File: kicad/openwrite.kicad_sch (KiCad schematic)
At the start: 147 parts, among them J1 raspberry-pi-zero-with-test-p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, SW71 SW_SPST, U1 kb2040, U2 powerboost-1000c, U3 waveshare-2in-lcd-st7789v

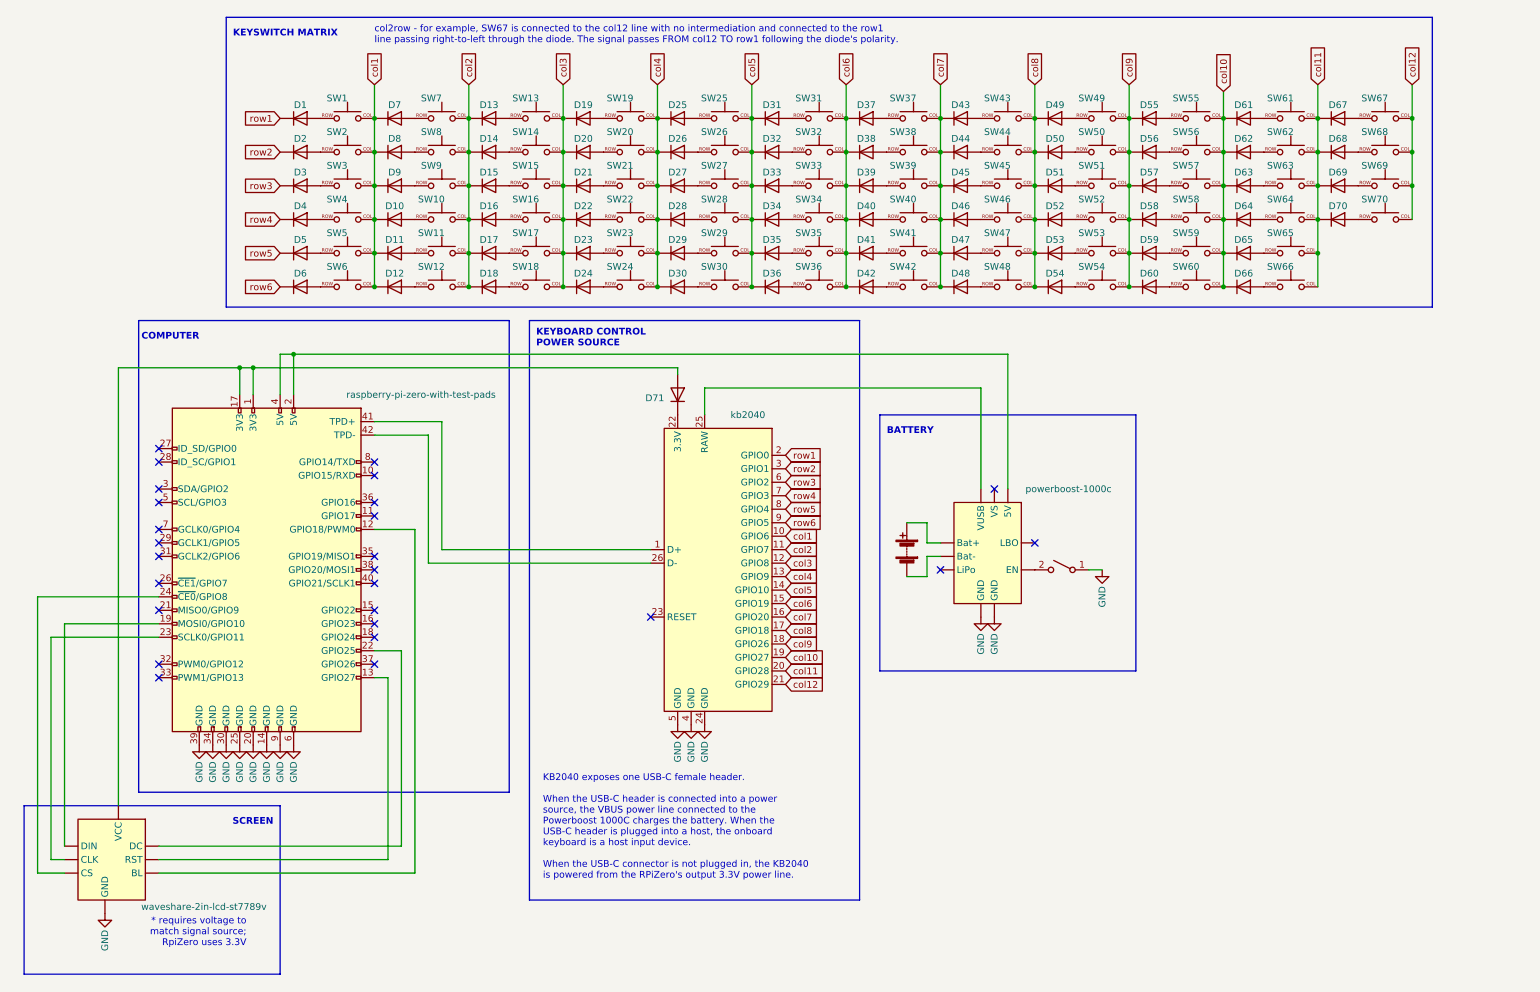
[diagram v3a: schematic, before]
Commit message: row connected to all row elements
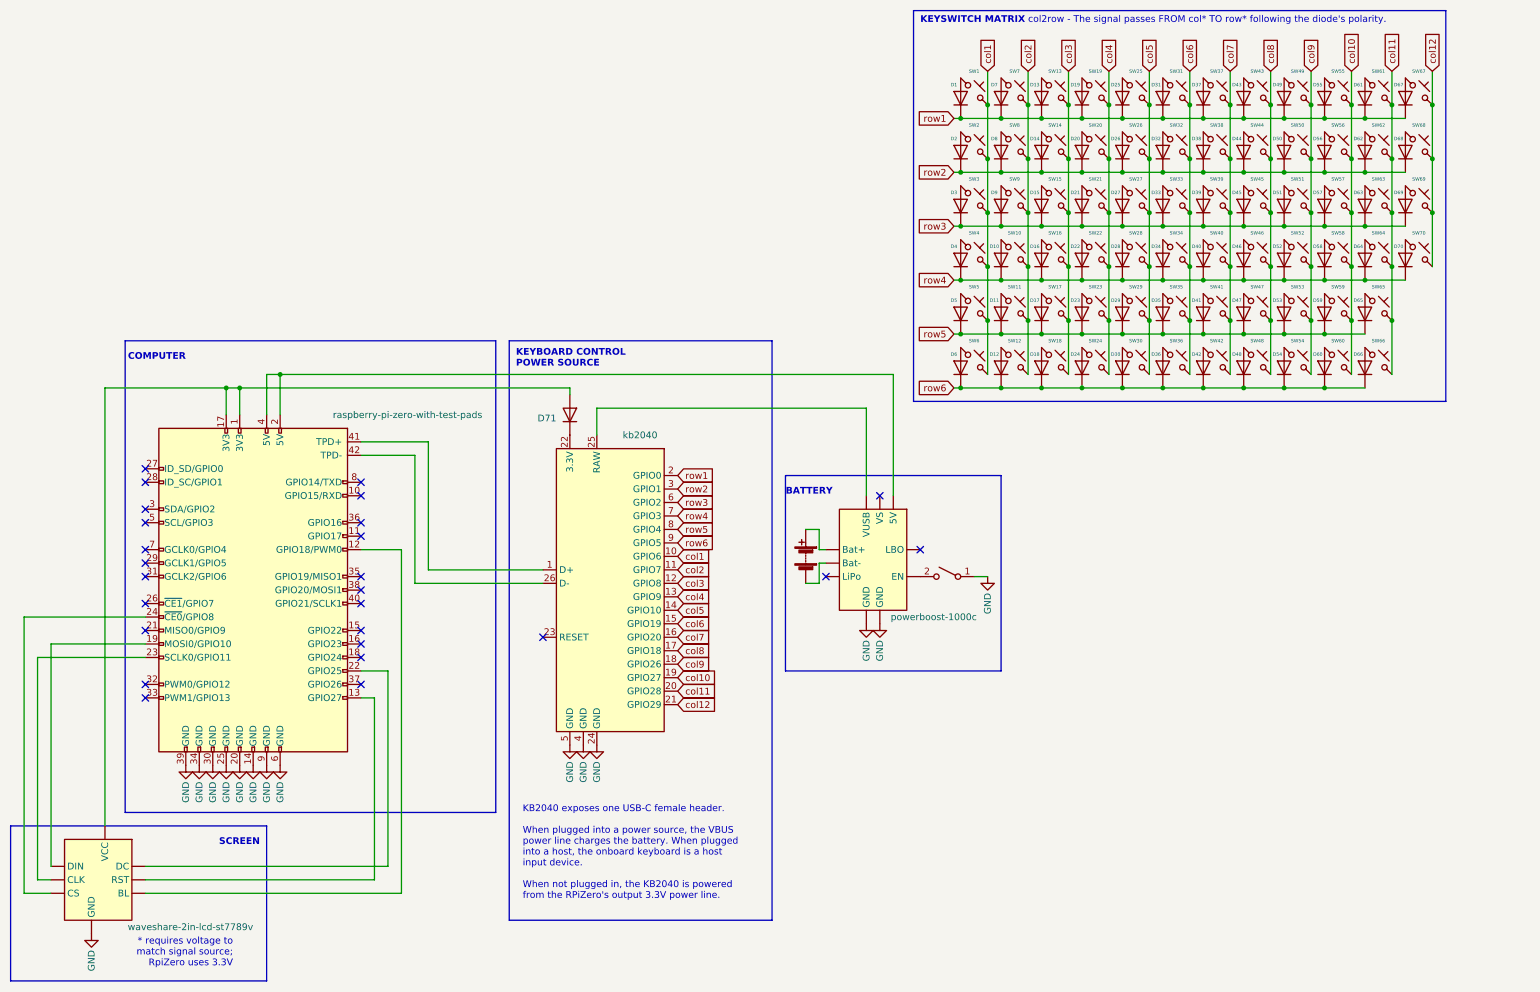
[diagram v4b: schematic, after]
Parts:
- D1, D10, D11, D12, D13, D14, D15, D16, D17, D18, D19, D2, D20, D21, D22, D23, D24, D25, D26, D27, D28, D29, D3, D30, D31, D32, D33, D34, D35, D36, D37, D38, D39, D4, D40, D41, D42, D43, D44, D45, D46, D47, D48, D49, D5, D50, D51, D52, D53, D54, D55, D56, D57, D58, D59, D6, D60, D61, D62, D63, D64, D65, D66, D67, D68, D69, D7, D70, D71, D8, D9: footprint Diode_THT:D_DO-35_SOD27_P7.62mm_Horizontal -> openwrite:diode-1N4148FS-ND
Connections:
- net col1: no longer D10.D1 (K), D11.D1 (K), D12.D1 (K), D7.D1 (K), D8.D1 (K), D9.D1 (K)
- net col10: no longer D61.D1 (K), D62.D1 (K), D63.D1 (K), D64.D1 (K), D65.D1 (K), D66.D1 (K)
- net col11: no longer D67.D1 (K), D68.D1 (K), D69.D1 (K), D70.D1 (K)
- net col2: no longer D13.D1 (K), D14.D1 (K), D15.D1 (K), D16.D1 (K), D17.D1 (K), D18.D1 (K)
- net col3: no longer D19.D1 (K), D20.D1 (K), D21.D1 (K), D22.D1 (K), D23.D1 (K), D24.D1 (K)
- net col4: no longer D25.D1 (K), D26.D1 (K), D27.D1 (K), D28.D1 (K), D29.D1 (K), D30.D1 (K)
- net col5: no longer D31.D1 (K), D32.D1 (K), D33.D1 (K), D34.D1 (K), D35.D1 (K), D36.D1 (K)
- net col6: no longer D37.D1 (K), D38.D1 (K), D39.D1 (K), D40.D1 (K), D41.D1 (K), D42.D1 (K)
- net col7: no longer D43.D1 (K), D44.D1 (K), D45.D1 (K), D46.D1 (K), D47.D1 (K), D48.D1 (K)
- net col8: no longer D49.D1 (K), D50.D1 (K), D51.D1 (K), D52.D1 (K), D53.D1 (K), D54.D1 (K)
- net col9: no longer D55.D1 (K), D56.D1 (K), D57.D1 (K), D58.D1 (K), D59.D1 (K), D60.D1 (K)
- net row1: now also D1.1, D13.1, D19.1, D25.1, D31.1, D37.1, D43.1, D49.1, D55.1, D61.1, D67.1, D7.1; no longer D1.D1 (K)
- net row2: now also D14.1, D2.1, D20.1, D26.1, D32.1, D38.1, D44.1, D50.1, D56.1, D62.1, D68.1, D8.1; no longer D2.D1 (K)
- net row3: now also D15.1, D21.1, D27.1, D3.1, D33.1, D39.1, D45.1, D51.1, D57.1, D63.1, D69.1, D9.1; no longer D3.D1 (K)
- net row4: now also D10.1, D16.1, D22.1, D28.1, D34.1, D4.1, D40.1, D46.1, D52.1, D58.1, D64.1, D70.1; no longer D4.D1 (K)
- net row5: now also D11.1, D17.1, D23.1, D29.1, D35.1, D41.1, D47.1, D5.1, D53.1, D59.1, D65.1; no longer D5.D1 (K)
- net row6: now also D12.1, D18.1, D24.1, D30.1, D36.1, D42.1, D48.1, D54.1, D6.1, D60.1, D66.1; no longer D6.D1 (K)
- net at SW29.ROW: now also D29.2; no longer D29.D2 (A)
- net at SW49.ROW: now also D49.2; no longer D49.D2 (A)
- net at SW70.ROW: now also D70.2; no longer D70.D2 (A)
- net at SW50.ROW: now also D50.2; no longer D50.D2 (A)
- net at SW15.ROW: now also D15.2; no longer D15.D2 (A)
- net at SW64.ROW: now also D64.2; no longer D64.D2 (A)
- net at SW47.ROW: now also D47.2; no longer D47.D2 (A)
- net at SW62.ROW: now also D62.2; no longer D62.D2 (A)
- net at SW40.ROW: now also D40.2; no longer D40.D2 (A)
- net at SW68.ROW: now also D68.2; no longer D68.D2 (A)
- net at SW2.ROW: now also D2.2; no longer D2.D2 (A)
- net at SW58.ROW: now also D58.2; no longer D58.D2 (A)
- net at SW26.ROW: now also D26.2; no longer D26.D2 (A)
- net at SW30.ROW: now also D30.2; no longer D30.D2 (A)
- net at SW51.ROW: now also D51.2; no longer D51.D2 (A)
- net at SW5.ROW: now also D5.2; no longer D5.D2 (A)
- net at SW16.ROW: now also D16.2; no longer D16.D2 (A)
- net at SW56.ROW: now also D56.2; no longer D56.D2 (A)
- net at SW35.ROW: now also D35.2; no longer D35.D2 (A)
- net at SW65.ROW: now also D65.2; no longer D65.D2 (A)
- net at SW23.ROW: now also D23.2; no longer D23.D2 (A)
- net at SW14.ROW: now also D14.2; no longer D14.D2 (A)
- net at SW55.ROW: now also D55.2; no longer D55.D2 (A)
- net at SW69.ROW: now also D69.2; no longer D69.D2 (A)
- net at SW63.ROW: now also D63.2; no longer D63.D2 (A)
- net at SW54.ROW: now also D54.2; no longer D54.D2 (A)
- net at SW53.ROW: now also D53.2; no longer D53.D2 (A)
- net at SW67.ROW: now also D67.2; no longer D67.D2 (A)
- net at SW48.ROW: now also D48.2; no longer D48.D2 (A)
- net at SW22.ROW: now also D22.2; no longer D22.D2 (A)
- net at SW11.ROW: now also D11.2; no longer D11.D2 (A)
- net at SW60.ROW: now also D60.2; no longer D60.D2 (A)
- net at SW34.ROW: now also D34.2; no longer D34.D2 (A)
- net at SW24.ROW: now also D24.2; no longer D24.D2 (A)
- net at SW61.ROW: now also D61.2; no longer D61.D2 (A)
- net at SW37.ROW: now also D37.2; no longer D37.D2 (A)
- net at SW31.ROW: now also D31.2; no longer D31.D2 (A)
- net at SW38.ROW: now also D38.2; no longer D38.D2 (A)
- net at SW8.ROW: now also D8.2; no longer D8.D2 (A)
- net at SW3.ROW: now also D3.2; no longer D3.D2 (A)
- net at SW21.ROW: now also D21.2; no longer D21.D2 (A)
- net at SW46.ROW: now also D46.2; no longer D46.D2 (A)
- net at SW9.ROW: now also D9.2; no longer D9.D2 (A)
- net at SW52.ROW: now also D52.2; no longer D52.D2 (A)
- net at SW20.ROW: now also D20.2; no longer D20.D2 (A)
- net at SW18.ROW: now also D18.2; no longer D18.D2 (A)
- net at SW32.ROW: now also D32.2; no longer D32.D2 (A)
- net at SW66.ROW: now also D66.2; no longer D66.D2 (A)
- net at SW28.ROW: now also D28.2; no longer D28.D2 (A)
- net at SW10.ROW: now also D10.2; no longer D10.D2 (A)
- net at U1.22 (3.3V): now also D71.1; no longer D71.D1 (K)
- net at SW25.ROW: now also D25.2; no longer D25.D2 (A)
- net at SW27.ROW: now also D27.2; no longer D27.D2 (A)
- net at SW17.ROW: now also D17.2; no longer D17.D2 (A)
- net at SW4.ROW: now also D4.2; no longer D4.D2 (A)
- net at J1.1 (3V3), J1.17 (3V3), U3. (VCC): now also D71.2; no longer D71.D2 (A)
- net at SW45.ROW: now also D45.2; no longer D45.D2 (A)
- net at SW33.ROW: now also D33.2; no longer D33.D2 (A)
- net at SW44.ROW: now also D44.2; no longer D44.D2 (A)
- net at SW19.ROW: now also D19.2; no longer D19.D2 (A)
- net at SW1.ROW: now also D1.2; no longer D1.D2 (A)
- net at SW57.ROW: now also D57.2; no longer D57.D2 (A)
- net at SW42.ROW: now also D42.2; no longer D42.D2 (A)
- net at SW12.ROW: now also D12.2; no longer D12.D2 (A)
- net at SW41.ROW: now also D41.2; no longer D41.D2 (A)
- net at SW59.ROW: now also D59.2; no longer D59.D2 (A)
- net at SW43.ROW: now also D43.2; no longer D43.D2 (A)
- net at SW36.ROW: now also D36.2; no longer D36.D2 (A)
- net at SW6.ROW: now also D6.2; no longer D6.D2 (A)
- net at SW39.ROW: now also D39.2; no longer D39.D2 (A)
- net at SW7.ROW: now also D7.2; no longer D7.D2 (A)
- net at SW13.ROW: now also D13.2; no longer D13.D2 (A)
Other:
- note added: "KB2040 exposes one USB-C female header. When plugged into a power source, the VBUS power line charges the battery. When plugged into a host, the onboard keyboard is a host input device. When not plugged in, the KB2040 is powered from the RPiZero's output 3.3V power line."
- note added: "col2row - The signal passes FROM col* TO row* following the diode's polarity."
- note removed: "KB2040 exposes one USB-C female header. When the USB-C header is connected into a power source, the VBUS power line connected to the Powerboost 1000C charges the battery. When the USB-C header is plugged into a host, the onboard keyboard is a host input device. When the USB-C connector is not plugged in, the KB2040 is powered from the RPiZero's output 3.3V power line."
- note removed: "col2row - for example, SW67 is connected to the col12 line with no intermediation and connected to the row1 line passing right-to-left through the diode. The signal passes FROM col12 TO row1 following the diode's polarity."
- moved on the sheet: D1, D71
